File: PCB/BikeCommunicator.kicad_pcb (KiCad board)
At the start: 2 copper layers, 43.4 x 50 mm, 14 parts, among them SW1 SW_SPST_LED, SW2 SW_SPST_LED, SW3 SW_SPST_LED, SW4 SW_SPST_LED, U1 HW-108_DC-DC, U2 HTCC-AB01

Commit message: Fit PCB to housing, added some more elements to scheme
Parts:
- added BT1: Battery_Cell, Connector_Wire:SolderWirePad_1x02_P3.81mm_Drill1mm, F.Cu at (99.1, 97.0)
- added D1: D, Diodes_THT:D_A-405_P7.62mm_Horizontal, F.Cu at (108.2, 91.4)
- added J1: Barrel_Jack_Switch, Connectors:BARREL_JACK, F.Cu at (121.9, 91.4)
- added J2: USB_B_Micro, Connectors_USB:USB_Micro-B_Molex-105017-0001, F.Cu at (134.6, 97.3)
- added SW5: SW_DPDT_x2, Buttons_Switches_THT:SW_CuK_JS202011AQN_DPDT_Angled, F.Cu at (150.1, 54.4)
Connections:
- net GND renamed -BATT
- U1 pad 4: +5V -> Net-(SW5-Pad5)
- U2 pad 13: +3V3 -> +5V
- U2 pad 3: Net-(U2-Pad3) -> +3V3
- U2 pad 4: +5V -> Net-(U2-Pad4)
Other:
- board outline removed

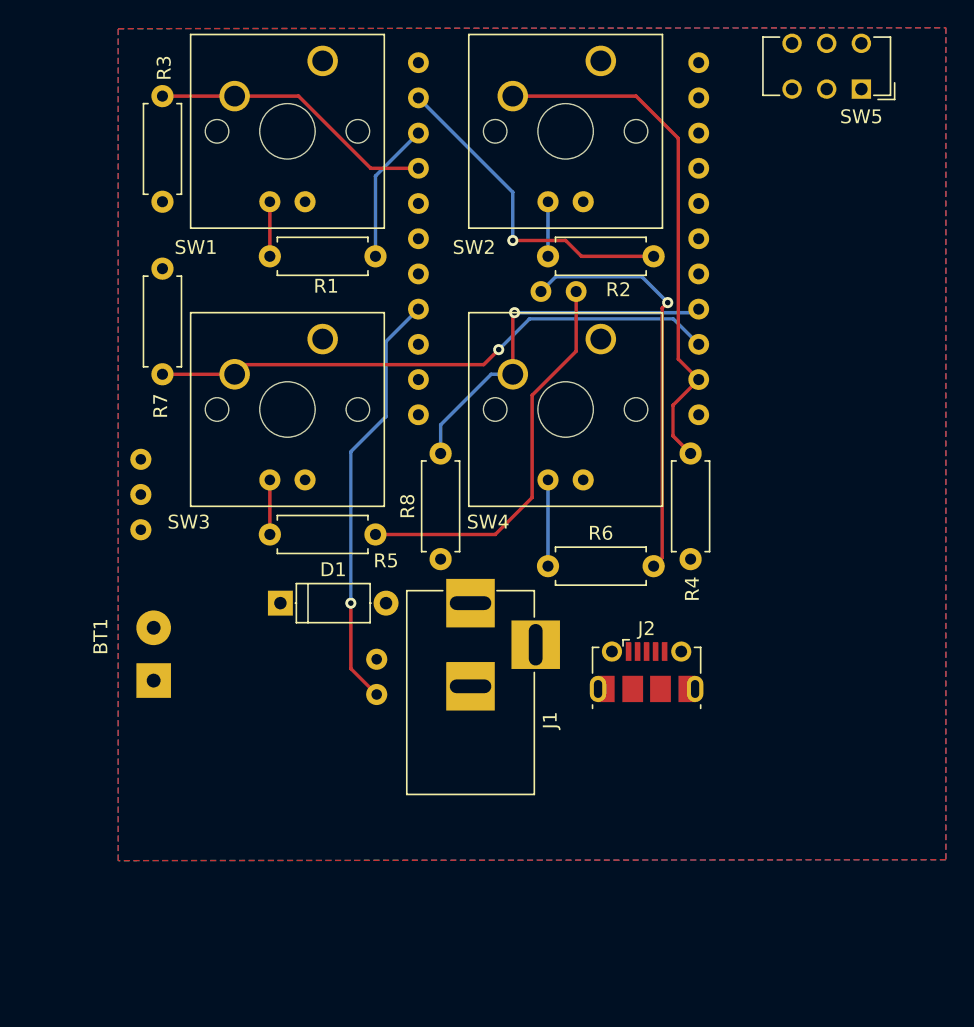
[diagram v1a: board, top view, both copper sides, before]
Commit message: Redesigned PCB and housing to fit it.
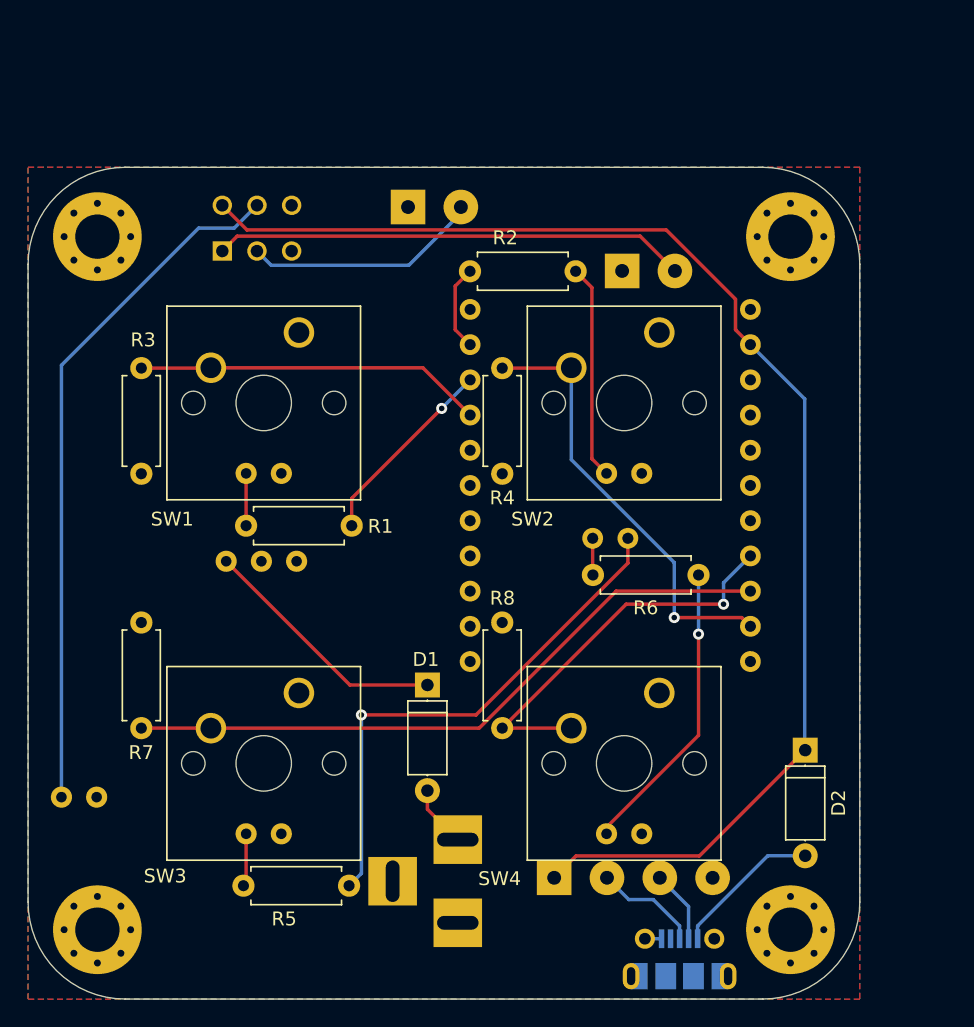
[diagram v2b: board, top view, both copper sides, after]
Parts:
- added D2: D, Diodes_THT:D_A-405_P7.62mm_Horizontal, F.Cu at (146.1, 102.0)
- added H1: MountingHole_Pad, MountingHole:MountingHole_3.2mm_M3_Pad_Via, F.Cu at (95.0, 65.0)
- added H2: MountingHole_Pad, MountingHole:MountingHole_3.2mm_M3_Pad_Via, F.Cu at (145.0, 65.0)
- added H3: MountingHole_Pad, MountingHole:MountingHole_3.2mm_M3_Pad_Via, F.Cu at (95.0, 115.0)
- added H4: MountingHole_Pad, MountingHole:MountingHole_3.2mm_M3_Pad_Via, F.Cu at (145.0, 115.0)
- added J3: Conn_01x04, Connector_Wire:SolderWirePad_1x04_P3.81mm_Drill1mm, B.Cu at (128.0, 111.3)
- added J4: Conn_01x02, Connector_Wire:SolderWirePad_1x02_P3.81mm_Drill1mm, F.Cu at (132.9, 67.5)
- added REF**: OSHW-Logo2_7.3x6mm_SilkScreen, Symbol:OSHW-Logo2_7.3x6mm_SilkScreen, B.Cu at (101.9, 81.2)
- J1, J2, SW5: moved to B.Cu
- moved SW5 47.6 mm to (104.0, 66.0), turned to 0 degrees
- moved BT1 38.8 mm to (117.4, 62.9), turned to 0 degrees
- moved SW4 25.9 mm to (135.5, 97.9)
- moved SW3 25.6 mm to (109.5, 97.9)
- moved R7 25.6 mm to (98.2, 92.8)
- moved R5 25.4 mm to (105.5, 111.8)
- moved J2 20.9 mm to (137.0, 118.0), turned to 180 degrees
- moved SW2 20.0 mm to (135.5, 71.9)
- moved R3 19.7 mm to (98.2, 82.1)
- moved SW1 19.7 mm to (109.5, 71.9)
- moved R1 19.5 mm to (105.7, 85.9)
- moved U2 18.2 mm to (132.0, 86.0)
- moved J1 17.1 mm to (121.0, 108.5)
- moved R4 14.9 mm to (124.2, 82.1)
- moved D1 12.1 mm to (118.8, 97.3), turned to 270 degrees
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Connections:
- J2 pad 1: +5V -> Net-(D2-Pad2)
- J2 pad 2: Net-(J2-Pad2) -> /USBD-
- J2 pad 3: Net-(J2-Pad3) -> /USBD+
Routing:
- net +5V: track 30.6 -> 96.4 mm, vias 1 -> 0
- net Net-(SW5-Pad5): track 0.00 -> 50.0 mm
- net +BATT: track 0.00 -> 34.1 mm
- net /LED4: track 29.8 -> 2.65 mm, vias 1 -> 0
- net +12V: track 0.00 -> 18.2 mm
- net /LED2: track 23.7 -> 6.18 mm, vias 1 -> 0
- net Net-(BT1-Pad1): track 0.00 -> 16.5 mm
- net Net-(R6-Pad1): track 6.22 -> 21.4 mm, vias 0 -> 1
- net Net-(R2-Pad1): track 3.94 -> 15.5 mm
- net Net-(D2-Pad2): track 0.00 -> 10.8 mm
- net /LED3: track 28.6 -> 38.2 mm, vias 0 -> 1
- net /USBD+: track 0.00 -> 7.60 mm
- net /BTN3: track 41.1 -> 48.0 mm, vias 1 -> 0
- net /BTN2: track 37.8 -> 31.8 mm, vias 0 -> 1
- net /USBD-: track 0.00 -> 5.26 mm
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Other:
- board outline added: 60 x 60 mm
- board text added: "+"
- board text added: "-"
- board text added: "5V"
- board text added: "5V IN"
- board text added: "BATT"
- board text added: "BATTERY IN 3,7V"
- board text added: "BATTERY SWITCHED"
- board text added: "Bike Communicator"
- board text added: "D+"
- board text added: "D-"
- board text added: "DCDC 12V -> 5V"
- board text added: "GND"
- board text added: "GZT project 2020"
- board text added: "UNREGULATED 12V IN"
- board text added: "USB"
- board text added: "rev 1.0"
- board text added: "www.gzt.si"

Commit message: Updated PCB project file
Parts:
- R1: value R -> 0R
- R2: value R -> 220R
- R3, R4, R7, R8: value R -> 4k7
- R5, R6: value R -> 120R
- SW1: value SW_SPST_LED -> SW_SPST_LED_Green
- SW2: value SW_SPST_LED -> SW_SPST_LED_Blue
- SW3: value SW_SPST_LED -> SW_SPST_LED_Yellow
- SW4: value SW_SPST_LED -> SW_SPST_LED_Red

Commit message: Major PCB fix
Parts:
- moved R6 1.51 mm to (137.1, 90.2)
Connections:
- U2 pad 10: /LED2 -> /LED1
- U2 pad 12: -BATT -> Net-(U2-Pad12)
- U2 pad 13: +5V -> /BTN2
- U2 pad 14: Net-(U2-Pad14) -> /BTN3
- U2 pad 15: Net-(U2-Pad15) -> /BTN4
- U2 pad 19: /BTN4 -> Net-(U2-Pad19)
- U2 pad 20: /BTN3 -> Net-(U2-Pad20)
- U2 pad 21: /BTN2 -> +5V
- U2 pad 22: Net-(U2-Pad22) -> -BATT
- U2 pad 9: /LED1 -> /LED2
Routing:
- net /BTN2: track 31.8 -> 18.2 mm, vias 1 -> 0
- net /BTN3: track 48.0 -> 57.4 mm
- net /BTN4: track 28.9 -> 35.0 mm, vias 1 -> 0
- net +5V: track 96.4 -> 98.9 mm
- net /LED1: track 14.1 -> 16.6 mm
- net /LED2: track 6.18 -> 8.72 mm
- net /LED3: track 38.2 -> 37.3 mm
- net Net-(R6-Pad1): track 21.4 -> 21.1 mm, vias 1 -> 0

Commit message: SMD components on PCB, fabrication files...
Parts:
- removed REF**: OSHW-Logo2_7.3x6mm_SilkScreen, Symbol:OSHW-Logo2_7.3x6mm_SilkScreen
- D1, D2: footprint Diodes_THT:D_A-405_P7.62mm_Horizontal -> Diodes_SMD:D_SMA; moved to B.Cu
- R1, R2, R3, R4, R5, R6, R7, R8: footprint Resistor_THT:R_Axial_DIN0207_L6.3mm_D2.5mm_P7.62mm_Horizontal -> Resistors_SMD:R_1206; moved to B.Cu
- moved R2 16.8 mm to (130.3, 84.3)
- moved R3 9.35 mm to (100.4, 73.0), turned to 270 degrees
- moved R4 9.35 mm to (126.4, 73.0), turned to 270 degrees
- moved R6 6.96 mm to (130.7, 93.1), turned to 90 degrees
- moved D1 6.64 mm to (117.1, 103.8)
- moved R7 6.55 mm to (100.4, 99.0)
- moved R8 6.55 mm to (126.4, 99.0)
- moved D2 4.38 mm to (146.1, 106.4)
- moved BT1 3.76 mm to (121.2, 62.6), turned to 180 degrees
- moved R5 2.25 mm to (107.2, 110.3)
- moved R1 2.16 mm to (107.2, 84.3)
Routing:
- net Net-(R2-Pad1): track 15.5 -> 2.19 mm
- net /LED2: track 8.72 -> 20.5 mm
- net Net-(R6-Pad1): track 21.1 -> 14.0 mm
- net +3V3: track 0.00 -> 4.80 mm, vias 0 -> 4
- net /BTN4: track 35.0 -> 30.4 mm
- net /BTN3: track 57.4 -> 53.3 mm
- net /LED3: track 37.3 -> 34.0 mm
- net +5V: track 98.9 -> 101.3 mm, vias 0 -> 1
- net /BTN1: track 25.1 -> 23.0 mm
- net /BTN2: track 18.2 -> 16.1 mm
- net Net-(D1-Pad2): track 4.44 -> 6.21 mm
- net Net-(R5-Pad1): track 3.82 -> 2.22 mm
- net Net-(R1-Pad1): track 3.77 -> 2.19 mm
- net +12V: track 18.2 -> 19.7 mm
- net /LED1: track 16.6 -> 18.0 mm, vias 1 -> 0
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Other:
- board text added: "rev 2.0"
- board text removed: "rev 1.0"
